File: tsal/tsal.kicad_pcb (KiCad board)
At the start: 2 copper layers, 34.3 x 52.1 mm, 20 parts, among them P1 TS+ (PreAIR), P2 TS-, P3 CONN_01X01, P4 CONN_01X01, P5 TS+ (PostAIR), P6 CONN_01X01, P7 CONN_01X01, U1 V36SE12004NRFA, U2 TL431

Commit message: TSAL board layout
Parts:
- removed C3: 10u, Capacitors_ThroughHole:CP_Radial_D5.0mm_P2.00mm
- removed C4: 1u, Capacitors_ThroughHole:C_Rect_L7.2mm_W5.5mm_P5.00mm_FKS2_FKP2_MKS2_MKP2
- removed P4, P6, P7: CONN_01X01, Wire_Pads:SolderWirePad_single_2mmDrill
- removed P5: TS+ (PostAIR), Wire_Pads:SolderWirePad_single_1mmDrill
- removed REF** (x4): MountingHole_3.2mm_M3, Mounting_Holes:MountingHole_3.2mm_M3
- added F2: 3A, SMD_Packages:SMD-1210_Pol, F.Cu at (132.1, 92.6)
- added G***: LOGO, UNCAMotorsports:UNCA Logo, B.Cu at (119.4, 92.1)
- added J1: Indicator, Pin_Headers:Pin_Header_Straight_1x02, F.Cu at (113.0, 85.7)
- added J2: GLV, Pin_Headers:Pin_Header_Straight_1x02, F.Cu at (127.6, 83.2)
- added J3: TSAL, Pin_Headers:Pin_Header_Straight_1x02, F.Cu at (132.1, 97.8)
- added MK1: Mounting_Hole, Mounting_Holes:MountingHole_3mm, F.Cu at (99.1, 98.4)
- added MK3: Mounting_Hole, Mounting_Holes:MountingHole_3mm, F.Cu at (133.3, 85.1)
- added Q1: Q_PMOS_GSD, UNCAMotorsports:SOT23-3, F.Cu at (113.7, 95.5)
- added R3: 1.2k, Resistors_SMD:R_0805_HandSoldering, F.Cu at (112.3, 98.4)
- added R4: 0R, Resistors_SMD:R_0805_HandSoldering, F.Cu at (125.7, 98.4)
- added R5: 1k, Resistors_SMD:R_0805_HandSoldering, F.Cu at (128.3, 98.4)
- added U3: TCMT1103, UNCAMotorsports:SSOP-4, F.Cu at (119.4, 97.2)
- added U4: BTS6133D, UNCAMotorsports:TO-252-5, F.Cu at (126.5, 88.6)
- C1: value 10u -> 10uF; footprint Capacitors_ThroughHole:CP_Radial_D5.0mm_P2.00mm -> Capacitors_SMD:C_0805_HandSoldering
- C2: value 1u -> 10uF; footprint Capacitors_ThroughHole:C_Rect_L7.2mm_W5.5mm_P5.00mm_FKS2_FKP2_MKS2_MKP2 -> Capacitors_SMD:C_0805_HandSoldering
- F1: value Fuse -> 3A; footprint Fuse_Holders_and_Fuses:Fuse_SMD1206_HandSoldering -> SMD_Packages:SMD-1210_Pol; moved to F.Cu
- P1, P2: footprint Wire_Pads:SolderWirePad_single_2mmDrill -> Wire_Pads:SolderWirePad_single_1mmDrill
- P3: value CONN_01X01 -> TS+ (PostAIR); footprint Wire_Pads:SolderWirePad_single_2mmDrill -> Wire_Pads:SolderWirePad_single_1mmDrill
- R1, R2: moved to F.Cu
- U1: value V36SE12004NRFA -> V7812W-500; footprint UNCAMotorsports:V36SE12004NRFA -> UNCAMotorsports:V78W-500
- U2: footprint TO_SOT_Packages_SMD:SOT-23_Handsoldering -> UNCAMotorsports:SOT23-3; moved to F.Cu
- moved P2 39.5 mm to (94.6, 90.8)
- moved C1 23.4 mm to (99.1, 86.4)
- moved C2 21.9 mm to (99.1, 91.4)
- moved R1 16.6 mm to (103.5, 96.5), turned to 90 degrees
- moved R2 16.4 mm to (106.0, 96.5), turned to 270 degrees
- moved U1 14.7 mm to (102.9, 87.6), turned to 90 degrees
- moved F1 13.4 mm to (113.0, 90.7), turned to 270 degrees
- moved P3 12.6 mm to (94.6, 95.9)
- moved P1 12.1 mm to (94.6, 85.1)
- moved U2 7.34 mm to (109.6, 95.5), turned to 180 degrees
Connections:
- C1 pad 2: GND -> GNDA
- C2 pad 1: Net-(C1-Pad1) -> Net-(C2-Pad1)
- C2 pad 2: GND -> GNDA
- F1 pad 1: Net-(C1-Pad1) -> Net-(F1-Pad1)
- P1 pad 1: Net-(F1-Pad2) -> Net-(C1-Pad1)
- P2 pad 1: GND -> GNDA
- P3 pad 1: Net-(C3-Pad1) -> Net-(P3-Pad1)
- R1 pad 1: Net-(P5-Pad1) -> Net-(P3-Pad1)
- R2 pad 2: GND -> GNDA
- U1 pad 2: Net-(U1-Pad2) -> GNDA
- U1 pad 3: GND -> Net-(C2-Pad1)
- U2 pad 1: Net-(U1-Pad2) -> Net-(Q1-Pad1)
- U2 pad 3: GND -> GNDA
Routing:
- net Net-(C2-Pad1): track 0.00 -> 19.8 mm
- net Net-(P5-Pad1): track 13.4 -> 0.00 mm
- net GND: track 0.00 -> 12.2 mm
- net Net-(F2-Pad2): track 0.00 -> 11.0 mm
- net Net-(P3-Pad1): track 0.00 -> 10.8 mm
- net Net-(F2-Pad1): track 0.00 -> 10.6 mm
- net Net-(U1-Pad2): track 8.27 -> 0.00 mm
- net Net-(J2-Pad2): track 0.00 -> 8.21 mm
- net Net-(Q1-Pad1): track 0.00 -> 6.46 mm
- net Net-(R4-Pad1): track 0.00 -> 4.81 mm
- net Net-(R4-Pad2): track 0.00 -> 3.32 mm
- net Net-(F1-Pad1): track 0.00 -> 3.18 mm
- net Net-(R3-Pad1): track 0.00 -> 2.79 mm
- net Net-(R5-Pad1): track 0.00 -> 2.72 mm
- net Net-(F1-Pad2): track 4.61 -> 2.33 mm
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- added copper zone on B.Cu, net GNDA
- added copper zone on F.Cu, net GNDA
- removed copper zone on B.Cu, net GND
- removed copper zone on F.Cu, net Net-(C1-Pad1)
- removed copper zone on F.Cu, net Net-(C3-Pad1)
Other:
- board size 34.3 x 52.1 mm -> 45.7 x 21 mm
- net class Default: via_dia 0.8 -> 0.6
- rule pad_to_mask_clearance: 0.2 -> 0
- board text added: "Designed By Paul Guenette May 10, 2017 Rev 1"
- board text added: "HIGH VOLTAGE"

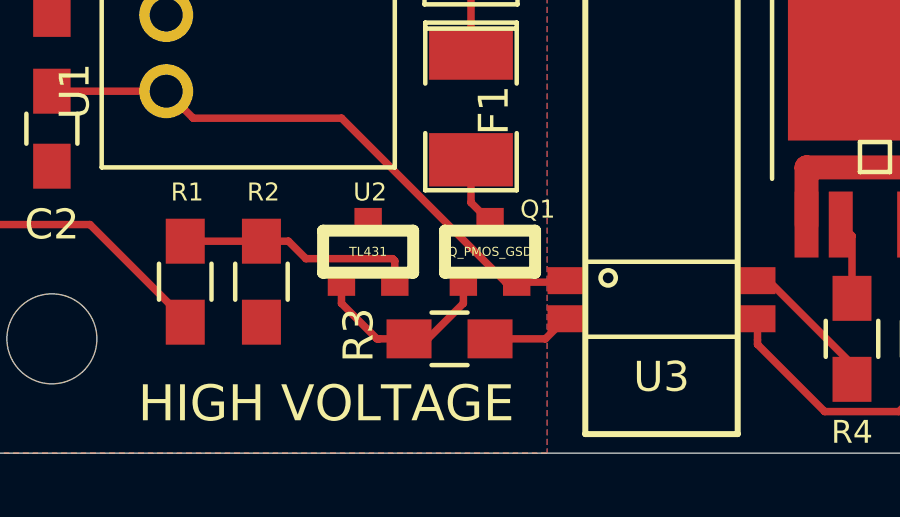
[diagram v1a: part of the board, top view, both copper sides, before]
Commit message: Changed position of resistor
The P-FET will now turn off reliably.
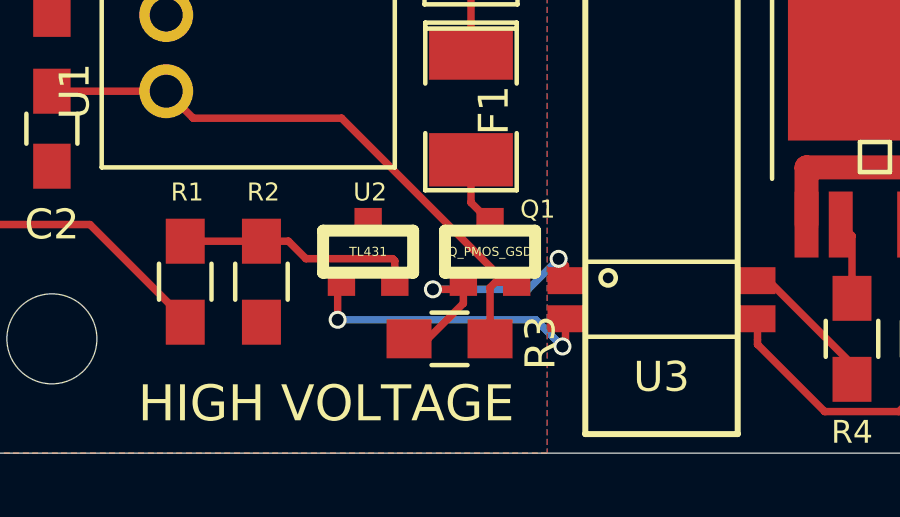
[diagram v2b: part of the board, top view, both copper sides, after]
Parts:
- turned R3 to 0 degrees
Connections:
- J2 pad 1: +12V -> (no net)
- R3 pad 1: Net-(R3-Pad1) -> Net-(Q1-Pad1)
- R3 pad 2: Net-(Q1-Pad1) -> Net-(C2-Pad1)
- U2 pad 1: Net-(Q1-Pad1) -> Net-(U2-Pad1)
- U3 pad 1: Net-(C2-Pad1) -> Net-(Q1-Pad1)
- U3 pad 2: Net-(R3-Pad1) -> Net-(U2-Pad1)
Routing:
- net Net-(U2-Pad1): track 0.00 -> 10.1 mm, vias 0 -> 2
- net Net-(Q1-Pad1): track 6.46 -> 9.63 mm, vias 0 -> 2
- net Net-(R3-Pad1): track 2.79 -> 0.00 mm
- net Net-(C2-Pad1): track 19.8 -> 20.8 mm
